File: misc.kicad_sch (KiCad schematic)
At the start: 53 parts, among them J10 Molex_KK_1x4_0470531000, J8 Molex_KK_1x4_0470531000, J9 Molex_KK_1x4_0470531000, Q1 MMBT3904LT1G, Q10 BSS138PW, Q11 PJE138K, Q12 PJE138K, Q2 MMBT3904LT1G, Q9 BSS84AKW, U18 ADT7476AARQZ, U19 74LVC1G157-Q100H_SOT457, U20 74LVC1G157-Q100H_SOT457, U21 NTS0102_TSSOP, U22 NTS0102_TSSOP, U23 NTS0102_TSSOP

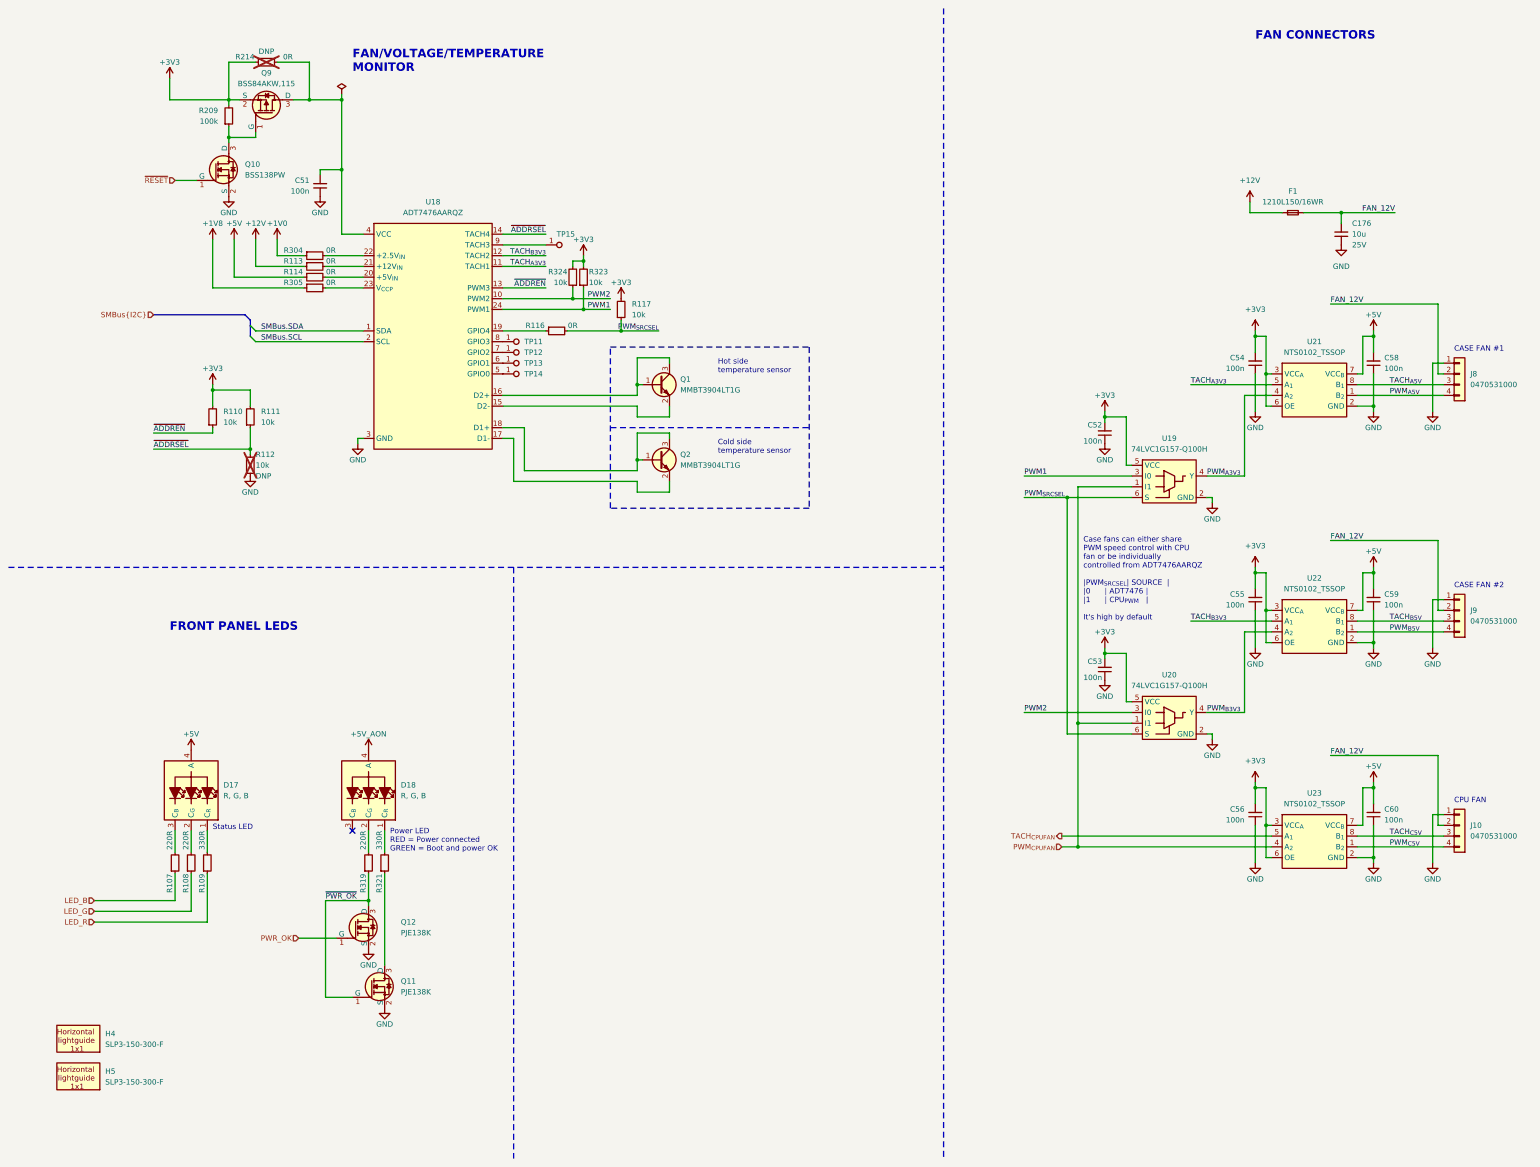
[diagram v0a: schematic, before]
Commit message: Reannotate schematic
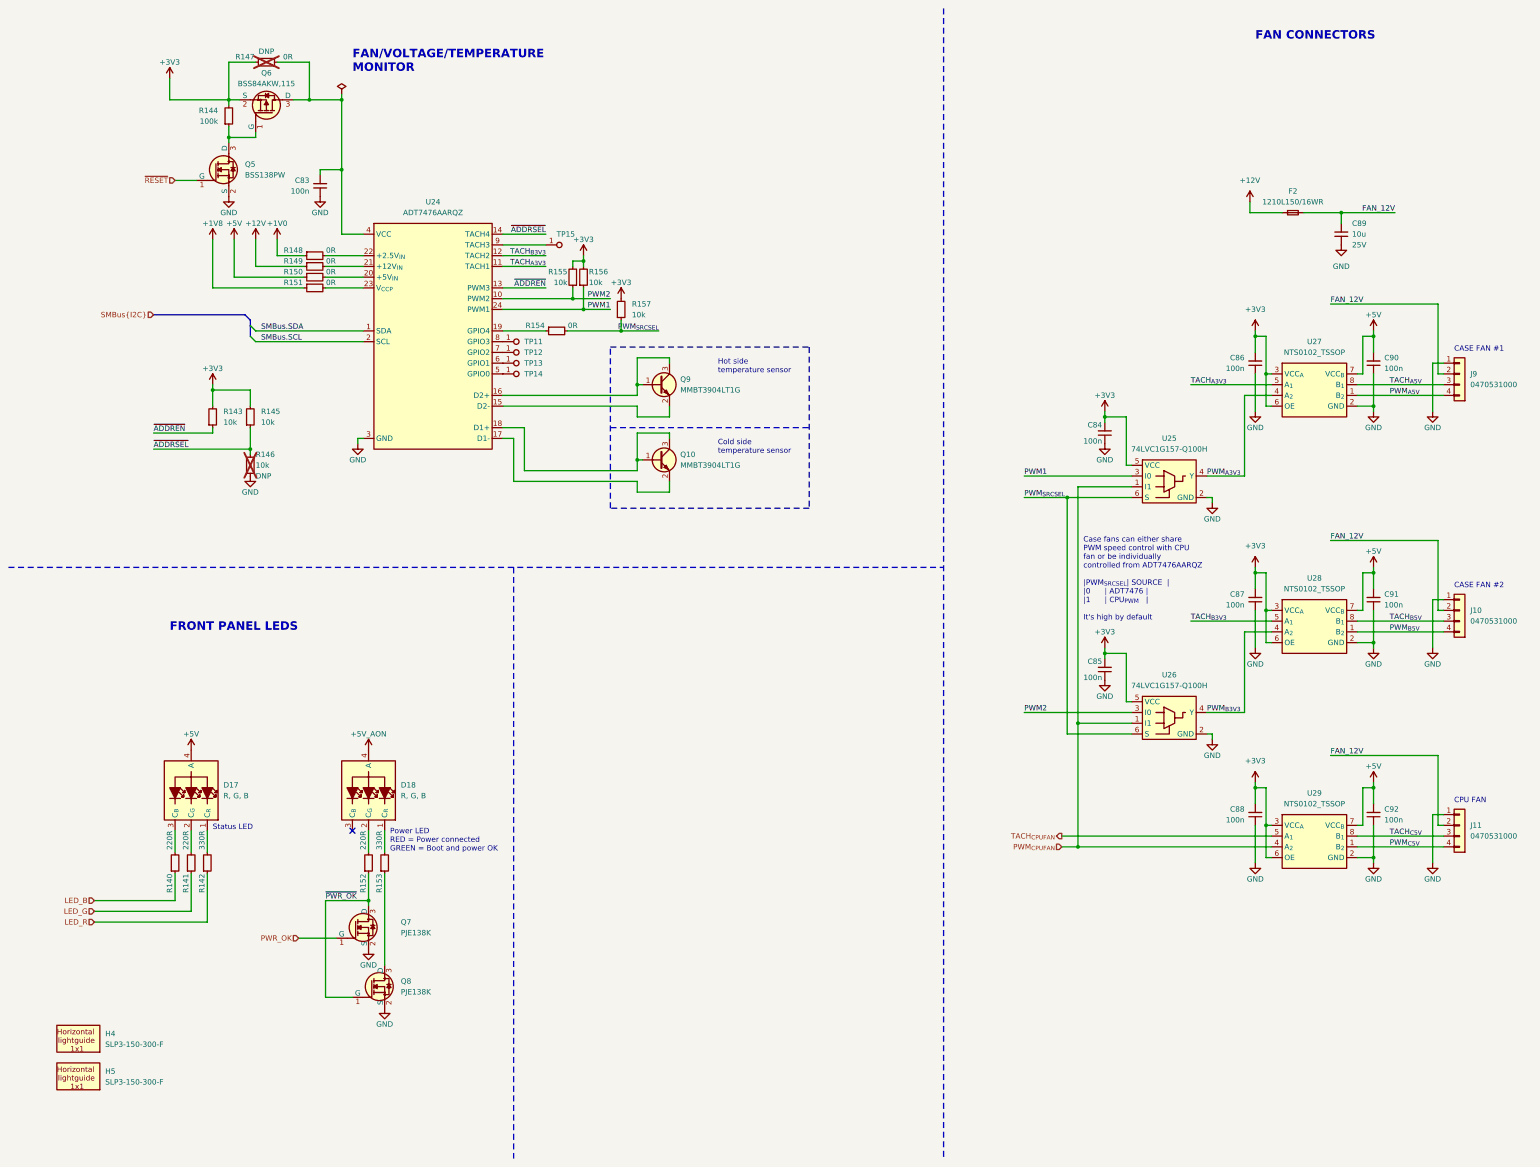
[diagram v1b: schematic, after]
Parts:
- renumbered C51 to C83, C52 to C84, C53 to C85, C54 to C86, C55 to C87, C56 to C88, C176 to C89, C58 to C90, C59 to C91, C60 to C92, F1 to F2, J9 to J10, J10 to J11, J8 to J9, Q2 to Q10, Q10 to Q5, Q9 to Q6, Q12 to Q7, Q11 to Q8, Q1 to Q9, R107 to R140, R108 to R141, R109 to R142, R110 to R143, R209 to R144, R111 to R145, R112 to R146, R214 to R147, R304 to R148, R113 to R149, R114 to R150, R305 to R151, R319 to R152, R321 to R153, R116 to R154, R324 to R155, R323 to R156, R117 to R157, U18 to U24, U19 to U25, U20 to U26, U21 to U27, U22 to U28, U23 to U29

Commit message: Optimize BOM, reannotate
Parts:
- removed C89: C_10u_25V_0603, antmicro-footprints:C_0603_1608Metric, symbol antmicroCapacitors0603:C_10u_25V_0603
- removed Q5: BSS138PW, antmicro-footprints:SC70-3, symbol antmicroTransistorsFETsMOSFETsSingle:BSS138PW
- removed Q7, Q8: PJE138K, antmicro-footprints:SOT-523, symbol antmicroTransistorsFETsMOSFETsSingle:PJE138K
- added C89: C_22u_16V_0603, antmicro-footprints:C_0603_1608Metric, symbol antmicroCapacitors0603:C_22u_16V_0603
- added Q5, Q7, Q8: BSS138-7-F, antmicro-footprints:SOT-23-3, symbol antmicroTransistorsFETsMOSFETsSingle:BSS138-7-F
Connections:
- net FAN_12V: now also C89.2
- net GND: now also C89.1, Q5.2 (S), Q7.2 (S), Q8.2 (S)
- net PWR_OK: now also Q7.1 (G)
- net ~{PWR_OK}: now also Q7.3 (D), Q8.1 (G)
- net ~{RESET}: now also Q5.1 (G)
- net at Q6.1 (G), R144.1: now also Q5.3 (D)
- net at R153.1: now also Q8.3 (D)

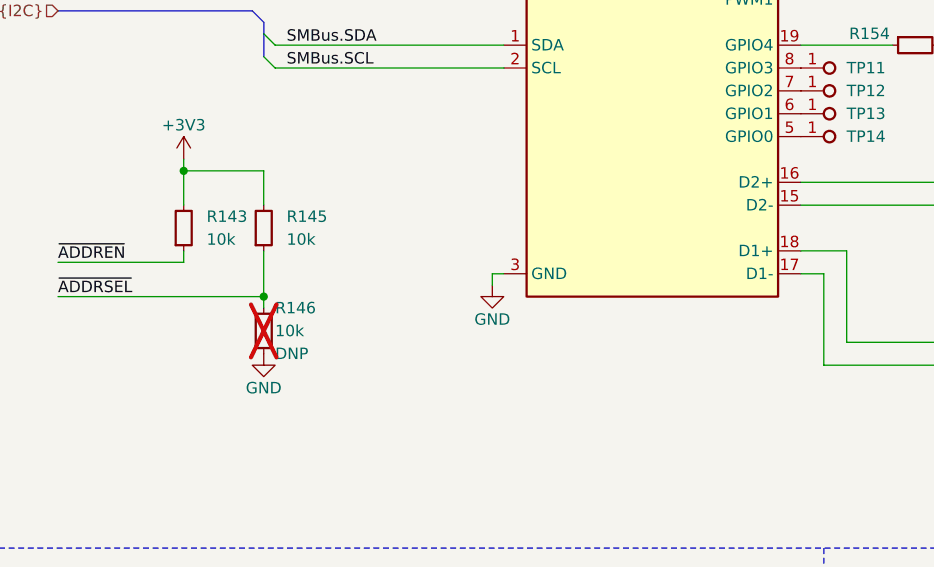
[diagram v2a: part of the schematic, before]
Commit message: [#58137] Add power monitors; clean up I2C bus
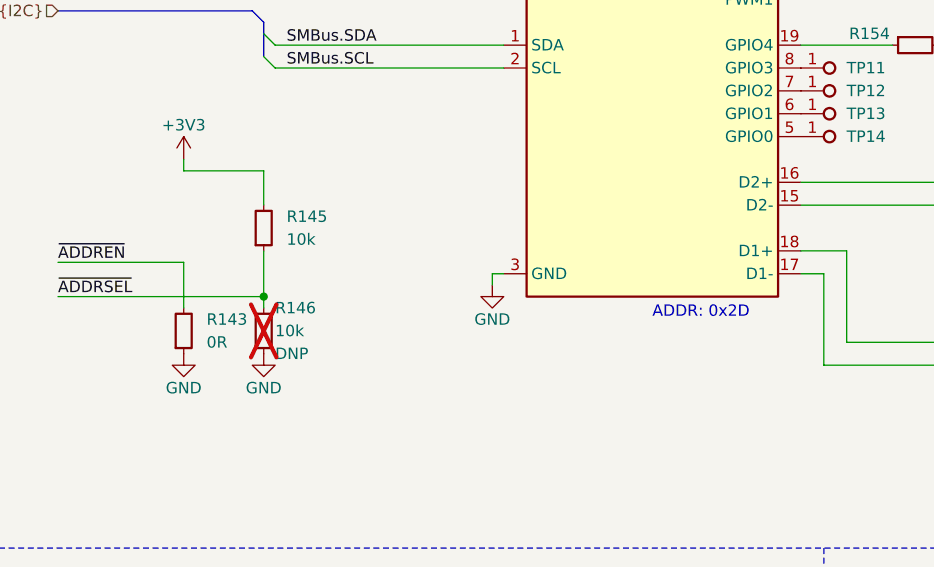
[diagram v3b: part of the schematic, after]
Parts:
- removed R143: R_10k_0402, antmicro-footprints:R_0402_1005Metric, symbol antmicroResistors0402:R_10k_0402
- added R143: R_0R_0402, antmicro-footprints:R_0402_1005Metric, symbol antmicroResistors0402:R_0R_0402
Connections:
- net GND: now also R143.1
- net ~{ADDREN}: now also R143.2
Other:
- note added: "ADDR: 0x2D"
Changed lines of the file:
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@@
   (junction (at 271.78 109.22) (diameter 0) (color 0 0 0 0)
   )
-  (junction (at 60.96 102.87) (diameter 0) (color 0 0 0 0)
-  )
   (junction (at 328.93 60.96) (diameter 0) (color 0 0 0 0)
   )
@@
     (stroke (width 0) (type default))
   )
-  (wire (pts (xy 60.96 102.87) (xy 60.96 106.68))
-    (stroke (width 0) (type default))
-  )
   (wire (pts (xy 59.69 207.01) (xy 59.69 212.09))
     (stroke (width 0) (type default))
@@
     (stroke (width 0) (type default))
   )
+  (wire (pts (xy 60.96 113.03) (xy 60.96 118.11))
+    (stroke (width 0) (type default))
+  )
   (wire (pts (xy 351.79 154.94) (xy 350.52 154.94))
     (stroke (width 0) (type default))
@@
     (stroke (width 0) (type default))
   )
-  (wire (pts (xy 60.96 111.76) (xy 60.96 113.03))
-    (stroke (width 0) (type default))
-  )
   (wire (pts (xy 168.91 114.3) (xy 168.91 113.03))
     (stroke (width 0) (type default))
@@
     (effects (font (size 1.27 1.27)) (justify left bottom))
   )
+  (text "ADDR: 0x2D" (at 113.03 119.38 0)
+    (effects (font (size 1.27 1.27)) (justify left bottom))
+  )
   (text "Hot side \ntemperature sensor" (at 180.34 99.06 0)
     (effects (font (size 1.27 1.27)) (justify left bottom))
@@
     )
   )
+  (symbol (lib_id "antmicroResistors0402:R_0R_0402") (at 60.96 123.19 90) (unit 1)
+    (in_bom yes) (on_board yes) (dnp no) (fields_autoplaced)
+    (property "Reference" "R143" (at 63.5 119.3799 90)
+      (effects (font (size 1.27 1.27) (thickness 0.15)) (justify right))
+    )
+    (property "Value" "R_0R_0402" (at 73.66 102.87 0)
+      (effects (font (size 1.27 1.27) (thickness 0.15)) (justify left bottom) hide)
+    )
+    (property "Footprint" "antmicro-footprints:R_0402_1005Metric" (at 76.2 102.87 0)
+      (effects (font (size 1.27 1.27) (thickness 0.15)) (justify left bottom) hide)
+    )
+    (property "Datasheet" "https://industrial.panasonic.com/cdbs/www-data/pdf/RDA0000/AOA0000C301.pdf" (at 78.74 102.87 0)
+      (effects (font (size 1.27 1.27) (thickness 0.15)) (justify left bottom) hide)
+    )
+    (property "MPN" "ERJ2GE0R00X" (at 81.28 102.87 0)
+      (effects (font (size 1.27 1.27) (thickness 0.15)) (justify left bottom) hide)
+    )
+    (property "Manufacturer" "Panasonic" (at 83.82 102.87 0)
+      (effects (font (size 1.27 1.27) (thickness 0.15)) (justify left bottom) hide)
+    )
+    (property "License" "Apache-2.0" (at 86.36 102.87 0)
+      (effects (font (size 1.27 1.27) (thickness 0.15)) (justify left bottom) hide)
+    )
+    (property "Author" "Antmicro" (at 88.9 102.87 0)
+      (effects (font (size 1.27 1.27) (thickness 0.15)) (justify left bottom) hide)
+    )
+    (property "Val" "0R" (at 63.5 121.9199 90)
+      (effects (font (size 1.27 1.27) (thickness 0.15)) (justify right))
+    )
+    (property "Tolerance" "~" (at 71.12 102.87 0)
+      (effects (font (size 1.27 1.27)) (justify left bottom) hide)
+    )
+    (property "Current" "1A" (at 91.44 102.87 0)
+      (effects (font (size 1.27 1.27) (thickness 0.15)) (justify left bottom) hide)
+    )
+    (pin "2")
+    (pin "1")
+    (instances
+      (project "com-express-7-baseboard"
+        (path "/1b8c34da-dad5-4b0b-8c4b-45db766c4dfa/6b3add4d-2eb4-4113-80da-1e75f64fe486"
+          (reference "R143") (unit 1)
+        )
+      )
+    )
+  )
   (symbol (lib_id "antmicroResistors0402:R_0R_0402") (at 82.55 76.2 0) (unit 1)
     (in_bom yes) (on_board yes) (dnp no)
@@
     )
   )
+  (symbol (lib_id "antmicropower:GND") (at 60.96 123.19 0) (unit 1)
+    (in_bom yes) (on_board yes) (dnp no)
+    (property "Reference" "#PWR0440" (at 69.85 125.73 0)
+      (effects (font (size 1.27 1.27) (thickness 0.15)) (justify left bottom) hide)
+    )
+    (property "Value" "GND" (at 60.96 127 0)
+      (effects (font (size 1.27 1.27) (thickness 0.15)))
+    )
+    (property "Footprint" "" (at 69.85 130.81 0)
+      (effects (font (size 1.27 1.27) (thickness 0.15)) (justify left bottom) hide)
+    )
+    (property "Datasheet" "" (at 69.85 135.89 0)
+      (effects (font (size 1.27 1.27) (thickness 0.15)) (justify left bottom) hide)
+    )
+    (property "Author" "Antmicro" (at 69.85 130.81 0)
+      (effects (font (size 1.27 1.27) (thickness 0.15)) (justify left bottom) hide)
+    )
+    (property "License" "Apache-2.0" (at 69.85 133.35 0)
+      (effects (font (size 1.27 1.27) (thickness 0.15)) (justify left bottom) hide)
+    )
+    (pin "1")
+    (instances
+      (project "com-express-7-baseboard"
+        (path "/1b8c34da-dad5-4b0b-8c4b-45db766c4dfa/6b3add4d-2eb4-4113-80da-1e75f64fe486"
+          (reference "#PWR0440") (unit 1)
+        )
+      )
+    )
+  )
   (symbol (lib_id "antmicropower:GND") (at 101.6 251.46 0) (mirror y) (unit 1)
     (in_bom yes) (on_board yes) (dnp no)
@@
         )
       )
-    )
-  )
-  (symbol (lib_id "antmicroResistors0402:R_10k_0402") (at 60.96 111.76 90) (unit 1)
-    (in_bom yes) (on_board yes) (dnp no) (fields_autoplaced)
-    (property "Reference" "R143" (at 63.5 107.95 90)
-      (effects (font (size 1.27 1.27) (thickness 0.15)) (justify right))
-    )
-    (property "Value" "R_10k_0402" (at 73.66 91.44 0)
-      (effects (font (size 1.27 1.27) (thickness 0.15)) (justify left bottom) hide)
-    )
-    (property "Footprint" "antmicro-footprints:R_0402_1005Metric" (at 76.2 91.44 0)
-      (effects (font (size 1.27 1.27) (thickness 0.15)) (justify left bottom) hide)
-    )
-    (property "Datasheet" "https://www.bourns.com/docs/product-datasheets/cr.pdf" (at 78.74 91.44 0)
-      (effects (font (size 1.27 1.27) (thickness 0.15)) (justify left bottom) hide)
-    )
-    (property "MPN" "CR0402-FX-1002GLF" (at 81.28 91.44 0)
-      (effects (font (size 1.27 1.27) (thickness 0.15)) (justify left bottom) hide)
-    )
-    (property "Manufacturer" "Bourns" (at 83.82 91.44 0)
-      (effects (font (size 1.27 1.27) (thickness 0.15)) (justify left bottom) hide)
-    )
-    (property "License" "Apache-2.0" (at 86.36 91.44 0)
-      (effects (font (size 1.27 1.27) (thickness 0.15)) (justify left bottom) hide)
-    )
-    (property "Author" "Antmicro" (at 88.9 91.44 0)
-      (effects (font (size 1.27 1.27) (thickness 0.15)) (justify left bottom) hide)
-    )
-    (property "Val" "10k" (at 63.5 110.49 90)
-      (effects (font (size 1.27 1.27) (thickness 0.15)) (justify right))
-    )
-    (property "Tolerance" "1%" (at 71.12 91.44 0)
-      (effects (font (size 1.27 1.27)) (justify left bottom) hide)
-    )
-    (pin "1")
-    (pin "2")
-    (instances
-      (project "com-express-7-baseboard"
-        (path "/1b8c34da-dad5-4b0b-8c4b-45db766c4dfa/6b3add4d-2eb4-4113-80da-1e75f64fe486"
-          (reference "R143") (unit 1)
-        )
-      )
